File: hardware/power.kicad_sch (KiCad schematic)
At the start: 69 parts, among them Q1 BSN20, Q2 AO3415A, U3 SY8088, U4 SY8088, U5 SY8088, U6 SY8089A, U7 SY8113, U8 SY8088

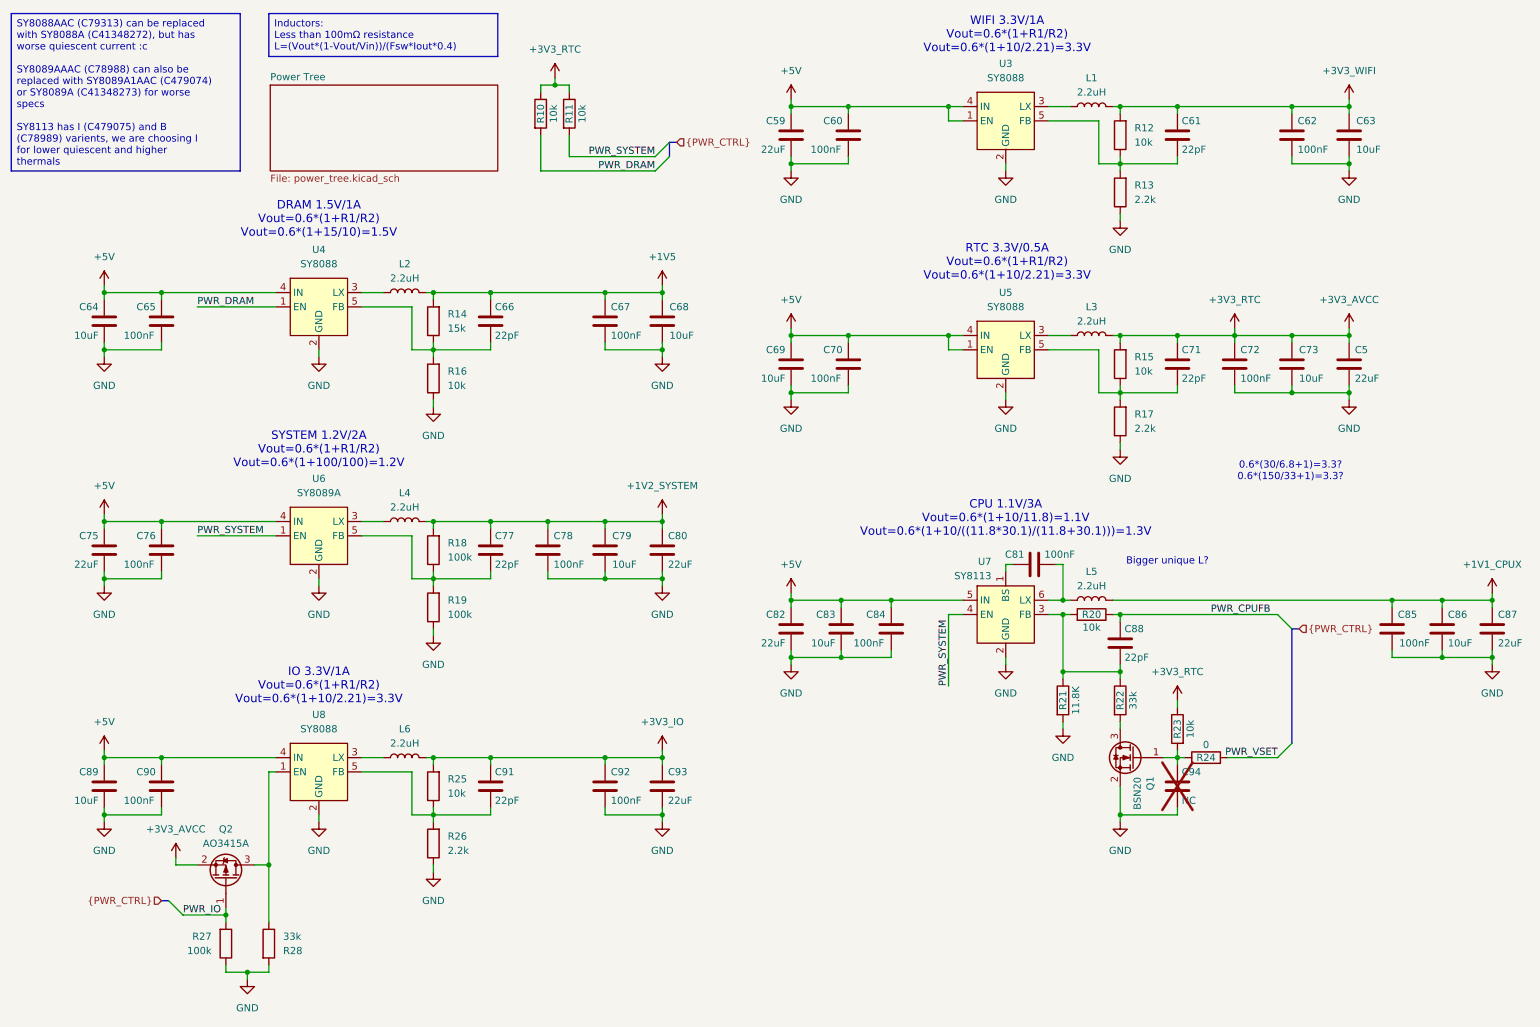
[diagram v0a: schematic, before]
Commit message: Improve routing and add test pads
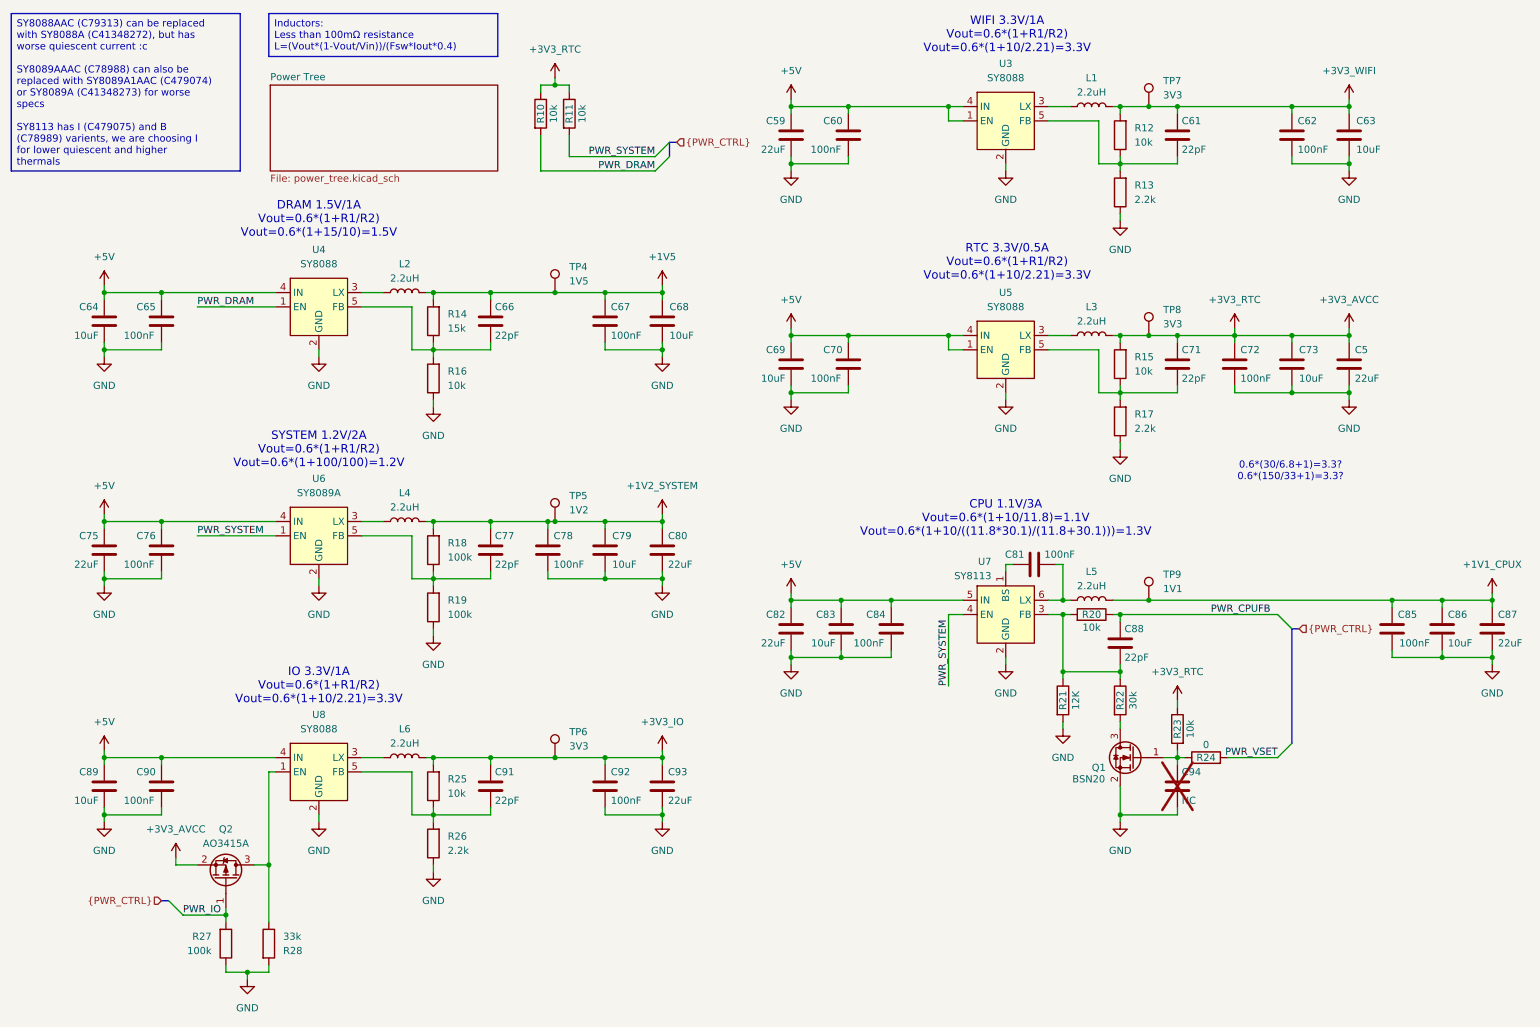
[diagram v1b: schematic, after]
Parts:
- added TP4: 1V5, TestPoint:TestPoint_Pad_D1.0mm, symbol Connector:TestPoint
- added TP5: 1V2, TestPoint:TestPoint_Pad_D1.0mm, symbol Connector:TestPoint
- added TP6, TP7, TP8: 3V3, TestPoint:TestPoint_Pad_D1.0mm, symbol Connector:TestPoint
- added TP9: 1V1, TestPoint:TestPoint_Pad_D1.0mm, symbol Connector:TestPoint
- L1, L2, L3, L6: LCSC Part # C19734 -> C43389
- R21: value 11.8K -> 12K; LCSC Part # C2929934 -> C25752
- R22: value 33k -> 30k; LCSC Part # C25779 -> C25553
- U7: FT Rotation Offset (none) -> 90
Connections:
- net +1V1_CPUX: now also TP9.1
- net +1V2_SYSTEM: now also TP5.1
- net +1V5: now also TP4.1
- net +3V3_AVCC: now also TP8.1
- net +3V3_IO: now also TP6.1
- net +3V3_WIFI: now also TP7.1
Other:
- note removed: "Bigger unique L?"

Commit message: Production ready
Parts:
- added C116, C117: 100nF, Capacitor_SMD:C_0402_1005Metric, symbol Device:C
- added TP10: PWR, TestPoint:TestPoint_Pad_D1.0mm, symbol Connector:TestPoint
- C61, C66, C71, C77, C88, C91: value 22pF -> 15pF; LCSC Part # C1555 -> C1548
- R28: value 33k -> 30k; LCSC Part # C25779 -> C25553
- TP4, TP5, TP6, TP7, TP8, TP9: now not fitted; now left out of the parts list
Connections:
- net +3V3_IO: now also C117.2
- net +3V3_WIFI: now also C116.2
- net +5V: now also C116.1, C117.1
- net PWR_VSET: now also TP10.1
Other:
- moved on the sheet: C94, R23, R24
